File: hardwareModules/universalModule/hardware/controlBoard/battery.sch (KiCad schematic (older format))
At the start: 27 parts

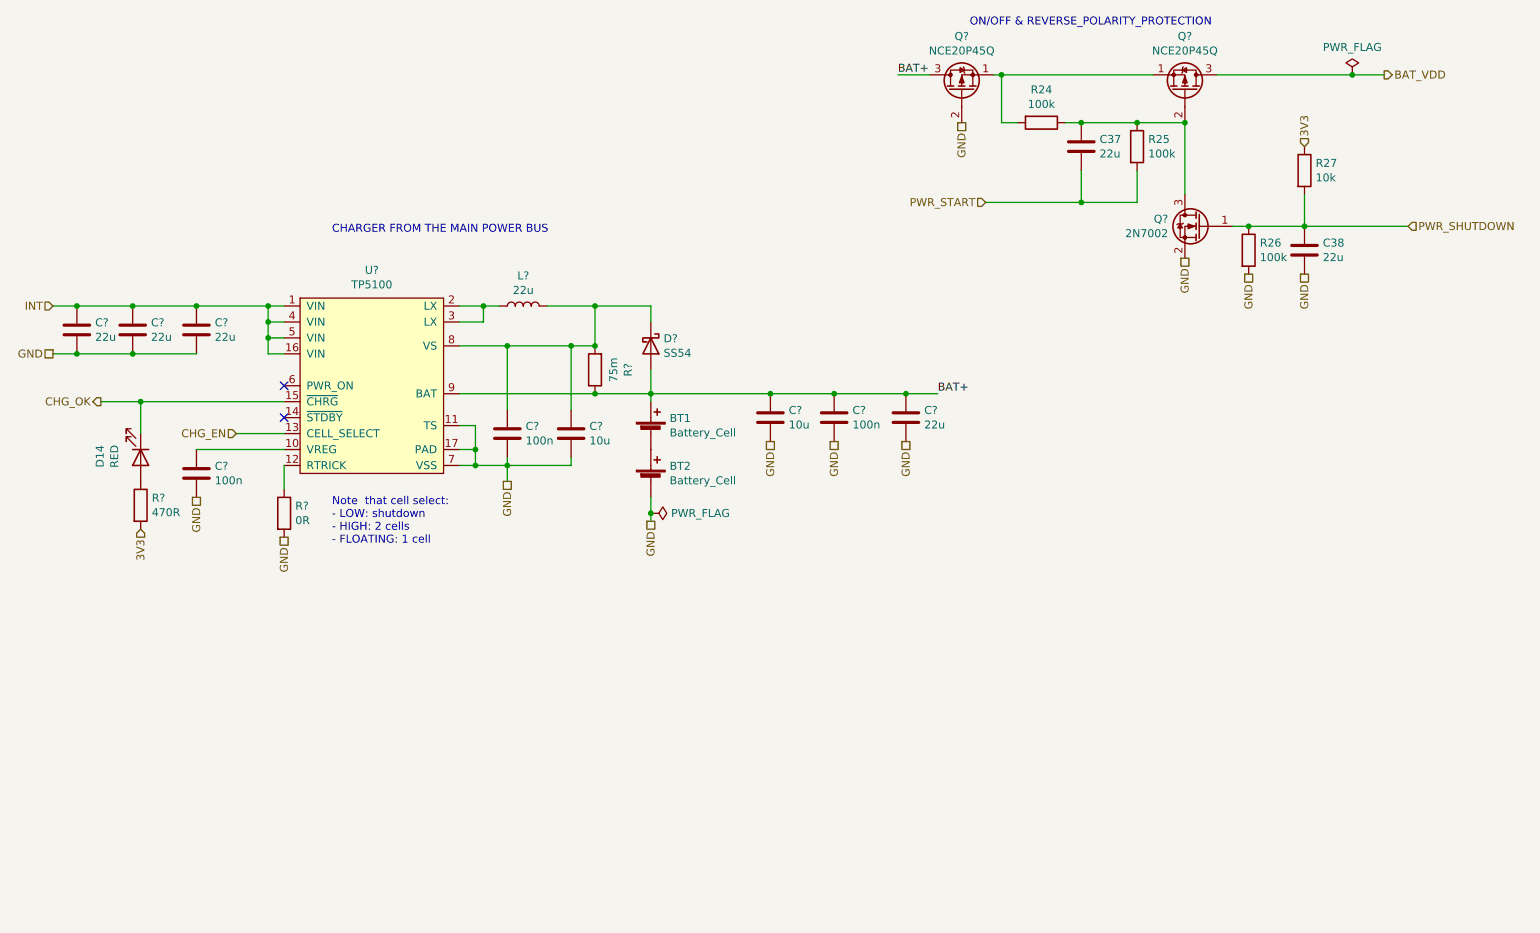
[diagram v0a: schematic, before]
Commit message: universalModule: Draft schematics of the new version of the control board
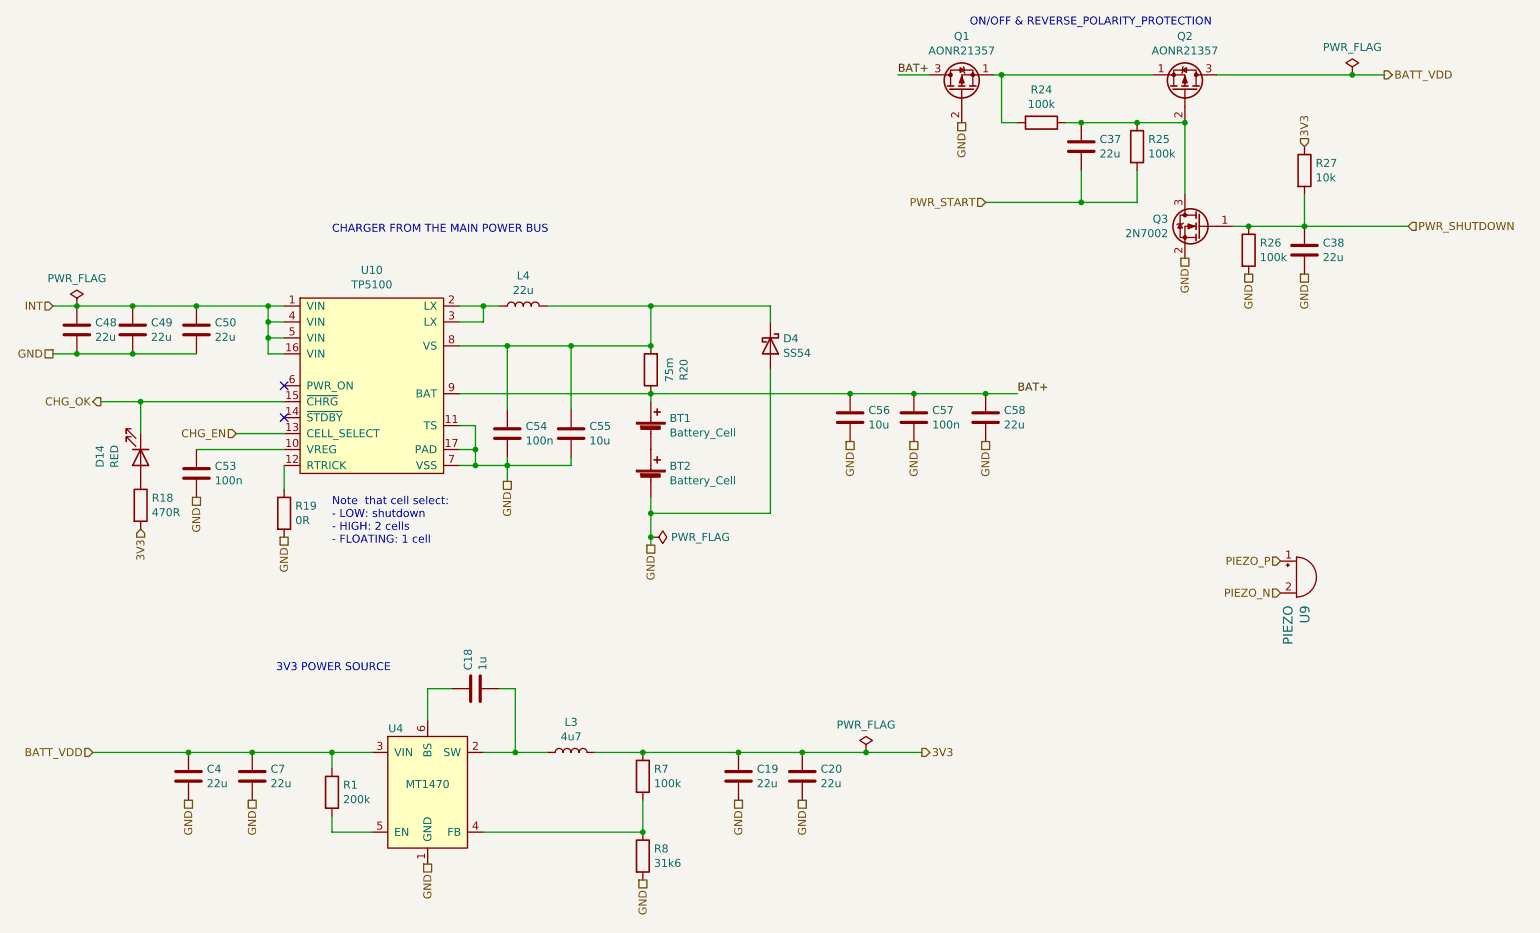
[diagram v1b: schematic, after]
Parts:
- added C18: 1u, Capacitor_SMD:C_0603_1608Metric, symbol Device:C
- added C19, C20, C4, C7: 22u, Capacitor_SMD:C_0805_2012Metric, symbol Device:C
- added L3: 4u7, rofi:SMNR5020, symbol Device:L
- added R1: 200k, Resistor_SMD:R_0402_1005Metric, symbol Device:R
- added R7: 100k, Resistor_SMD:R_0402_1005Metric, symbol Device:R
- added R8: 31k6, Resistor_SMD:R_0402_1005Metric, symbol Device:R
- added U4: MT1470, Package_TO_SOT_SMD:SOT-23-6, symbol rofi:MT1470
- added U9: PIEZO, rofi:CST-931AP, symbol Device:Buzzer
- Q1, Q2: renamed from Q?; value NCE20P45Q -> AONR21357; LCSC C193354 -> C431196
- R18: renamed from R?; footprint (none) -> Resistor_SMD:R_0402_1005Metric
- gave numbers to parts that had none: 15
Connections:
- net 3V3: now also C19.1, C20.1, L3.2, R7.1
- net BAT+: no longer D4.2 (A)
- net GND: now also D4.2 (A), C19.2, C20.2, C4.2, C7.2, R8.2, U4.1 (GND)
- net BAT_VDD renamed BATT_VDD
- net BATT_VDD: now also C4.1, C7.1, R1.1, U4.3 (VIN)
- new net: C18.1, U4.6 (BS)
- new net: C18.2, L3.1, U4.2 (SW)
- new net: R7.2, R8.1, U4.4 (FB)
- new net: R1.2, U4.5 (EN)
- new net PIEZO_N: U9.2 (+)
- new net PIEZO_P: U9.1 (-)
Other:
- note added: "3V3 POWER SOURCE"
- moved on the sheet: C56, C57, C58, D4, R20

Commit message: universalModule: Prepare electronics v0.2
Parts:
- removed C50: 22u, Capacitor_SMD:C_0805_2012Metric, symbol Device:C
- removed C56: 10u, Capacitor_SMD:C_0805_2012Metric, symbol Device:C
- BT1, BT2: #manf (none) -> 2x 1017-1; JLCPCB_IGNORE (none) -> YES
- C18: LCSC C52923 -> C15849
- D14, D4, Q3: JLCPCB_CORRECTION (none) -> 0;0;180
- Q1, Q2: JLCPCB_CORRECTION (none) -> 0;0;-90
- R19: LCSC (none) -> C17168
- R20: LCSC C57963 -> C127704
- R8: value 31k6 -> 22k; LCSC C11463 -> C25768
- U10: JLCPCB_CORRECTION (none) -> 0;0;-90; LCSC (none) -> C379389
- U4: value MT1470 -> SD8942; symbol rofi:MT1470 -> rofi:SD8942; JLCPCB_CORRECTION (none) -> 0;0;180; LCSC (none) -> C250795
- U9: JLCPCB_IGNORE (none) -> YES; MFR_QTY (none) -> 1
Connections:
- net BATT_VDD: now also U4.5 (VIN); no longer U4.3 (VIN)
- net GND: now also U4.2 (GND); no longer U4.1 (GND)
- net BATT_MID: now reaches BT1.2 (-), BT2.1 (+)
- net at C18.1: now also U4.1 (BS); no longer U4.6 (BS)
- net at C18.2, L3.1: now also U4.6 (SW); no longer U4.2 (SW)
- net at R7.2, R8.1: now also U4.3 (FB); no longer U4.4 (FB)
- net at R1.2: now also U4.4 (EN); no longer U4.5 (EN)
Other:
- moved on the sheet: BT2
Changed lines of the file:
@@
 $Descr A4 11693 8268
 encoding utf-8
-Sheet 5 5
+Sheet 5 14
 Title ""
 Date ""
@@
 F 3 "~" H 1950 4150 50  0001 C CNN
 F 4 "C2286" H 1950 4150 50  0001 C CNN "LCSC"
+F 5 "0;0;180" H 1950 4150 50  0001 C CNN "JLCPCB_CORRECTION"
 	1    1950 4150
 	0    1    1    0
@@
 Text HLabel 9250 3000 3    50   UnSpc ~ 0
 GND
-$Comp
-L Device:Q_PMOS_SGD Q2
-U 1 1 5FC760BF
-P 8500 1850
-F 0 "Q2" V 8842 1850 50  0000 C CNN
-F 1 "AONR21357" V 8751 1850 50  0000 C CNN
-F 2 "rofi:DFN3.3X3.3-EP" H 8700 1950 50  0001 C CNN
-F 3 "~" H 8500 1850 50  0001 C CNN
-F 4 "C431196" H 8500 1850 50  0001 C CNN "LCSC"
-	1    8500 1850
-	0    1    -1   0
-$EndComp
 Connection ~ 8500 2050
 $Comp
@@
 F 3 "~" H 7100 1850 50  0001 C CNN
 F 4 "C431196" H 7100 1850 50  0001 C CNN "LCSC"
+F 5 "0;0;-90" V 7100 1850 50  0001 C CNN "JLCPCB_CORRECTION"
 	1    7100 1850
 	0    -1   -1   0
@@
 F 3 "https://www.fairchildsemi.com/datasheets/2N/2N7002.pdf" H 8600 2700 50  0001 L CNN
 F 4 "C8545" H 8600 2700 50  0001 C CNN "LCSC"
+F 5 "0;0;180" H 8600 2700 50  0001 C CNN "JLCPCB_CORRECTION"
 	1    8600 2700
 	-1   0    0    -1
-$EndComp
-$Comp
-L Device:Battery_Cell BT2
-U 1 1 5DFAE964
-P 5150 4300
-F 0 "BT2" H 5268 4396 50  0000 L CNN
-F 1 "Battery_Cell" H 5268 4305 50  0000 L CNN
-F 2 "rofi:BATTERY_18350" V 5150 4360 50  0001 C CNN
-F 3 "~" V 5150 4360 50  0001 C CNN
-F 4 "" H 5150 4300 50  0001 C CNN "#manf"
-	1    5150 4300
-	1    0    0    -1
 $EndComp
 $Comp
@@
 F 2 "rofi:BATTERY_18350" V 5150 4060 50  0001 C CNN
 F 3 "~" V 5150 4060 50  0001 C CNN
-F 4 "" H 5150 4000 50  0001 C CNN "#manf"
+F 4 "2x 1017-1" H 5150 4000 50  0001 C CNN "#manf"
+F 5 "YES" H 5150 4000 50  0001 C CNN "JLCPCB_IGNORE"
 	1    5150 4000
 	1    0    0    -1
@@
 F 2 "Package_DFN_QFN:QFN-16-1EP_4x4mm_P0.65mm_EP2.1x2.1mm" H 3650 3100 50  0001 C CNN
 F 3 "" H 3650 3100 50  0001 C CNN
+F 4 "C379389" H 3400 3700 50  0001 C CNN "LCSC"
+F 5 "0;0;-90" H 3400 3700 50  0001 C CNN "JLCPCB_CORRECTION"
 	1    3400 3700
 	1    0    0    -1
@@
 F 2 "Resistor_SMD:R_1206_3216Metric" V 5080 3600 50  0001 C CNN
 F 3 "~" H 5150 3600 50  0001 C CNN
-F 4 "C57963" V 5150 3600 50  0001 C CNN "LCSC"
+F 4 "C127704" V 5150 3600 50  0001 C CNN "LCSC"
 	1    5150 3600
 	-1   0    0    1
@@
 Text HLabel 5150 4700 3    50   UnSpc ~ 0
 GND
-Wire Wire Line
-	5150 4400 5150 4500
 $Comp
 L power:PWR_FLAG #FLG0103
@@
 Wire Wire Line
 	5150 4650 5150 4700
-Wire Wire Line
-	5150 3800 5150 3750
 Connection ~ 5150 3750
 Text Label 7450 3750 0    50   ~ 0
@@
 F 3 "~" H 5900 3450 50  0001 C CNN
 F 4 "C22452" V 5900 3450 50  0001 C CNN "LCSC"
+F 5 "0;0;180" V 5900 3450 50  0001 C CNN "JLCPCB_CORRECTION"
 	1    5900 3450
 	0    1    1    0
@@
 $EndComp
 $Comp
-L Device:C C56
-U 1 1 5FD18536
-P 6400 3900
-F 0 "C56" H 6515 3946 50  0000 L CNN
-F 1 "10u" H 6515 3855 50  0000 L CNN
-F 2 "Capacitor_SMD:C_0805_2012Metric" H 6438 3750 50  0001 C CNN
-F 3 "~" H 6400 3900 50  0001 C CNN
-F 4 "C15850" H 6400 3900 50  0001 C CNN "LCSC"
-	1    6400 3900
-	1    0    0    -1
-$EndComp
-Connection ~ 6400 3750
-Wire Wire Line
-	6400 3750 6800 3750
-$Comp
 L Device:C C57
 U 1 1 5FD18C0D
@@
 Wire Wire Line
 	6800 3750 7250 3750
-Text HLabel 6400 4050 3    50   UnSpc ~ 0
-GND
 Text HLabel 6800 4050 3    50   UnSpc ~ 0
 GND
@@
 Text HLabel 2300 4400 3    50   UnSpc ~ 0
 GND
-$Comp
-L Device:C C50
-U 1 1 5FD4F2CC
-P 2300 3350
-F 0 "C50" H 2415 3396 50  0000 L CNN
-F 1 "22u" H 2415 3305 50  0000 L CNN
-F 2 "Capacitor_SMD:C_0805_2012Metric" H 2338 3200 50  0001 C CNN
-F 3 "~" H 2300 3350 50  0001 C CNN
-F 4 "GRM21BR61C226ME44L" H 2300 3350 50  0001 C CNN "#manf"
-F 5 "C45783" H 2300 3350 50  0001 C CNN "LCSC"
-	1    2300 3350
-	1    0    0    -1
-$EndComp
-$Comp
-L Device:C C49
-U 1 1 5FD4F8F1
-P 1900 3350
-F 0 "C49" H 2015 3396 50  0000 L CNN
-F 1 "22u" H 2015 3305 50  0000 L CNN
-F 2 "Capacitor_SMD:C_0805_2012Metric" H 1938 3200 50  0001 C CNN
-F 3 "~" H 1900 3350 50  0001 C CNN
-F 4 "GRM21BR61C226ME44L" H 1900 3350 50  0001 C CNN "#manf"
-F 5 "C45783" H 1900 3350 50  0001 C CNN "LCSC"
-	1    1900 3350
-	1    0    0    -1
-$EndComp
 $Comp
 L Device:C C48
@@
 Wire Wire Line
 	2850 3200 2750 3200
-Wire Wire Line
-	2300 3200 1900 3200
-Connection ~ 2300 3200
-Wire Wire Line
-	1900 3200 1550 3200
-Connection ~ 1900 3200
 Text HLabel 1400 3200 0    50   Input ~ 0
 INT
@@
 Connection ~ 1550 3200
 Wire Wire Line
-	2300 3500 1900 3500
-Wire Wire Line
-	1900 3500 1550 3500
-Connection ~ 1900 3500
-Wire Wire Line
 	1550 3500 1400 3500
-Connection ~ 1550 3500
 Text HLabel 1400 3500 0    50   UnSpc ~ 0
 GND
@@
 	2750 3300 2750 3200
 Connection ~ 2750 3200
-Wire Wire Line
-	2750 3200 2300 3200
 Wire Wire Line
 	2750 3300 2850 3300
@@
 F 2 "Resistor_SMD:R_0402_1005Metric" V 2780 4500 50  0001 C CNN
 F 3 "~" H 2850 4500 50  0001 C CNN
+F 4 "C17168" H 2850 4500 50  0001 C CNN "LCSC"
 	1    2850 4500
 	1    0    0    -1
@@
 PIEZO_N
 Wire Wire Line
-	5150 3750 6400 3750
-Wire Wire Line
 	5150 3200 5900 3200
 Wire Wire Line
@@
 F 2 "Capacitor_SMD:C_0603_1608Metric" H 4088 5450 50  0001 C CNN
 F 3 "~" H 4050 5600 50  0001 C CNN
-F 4 "C52923" H 4050 5600 50  0001 C CNN "LCSC"
+F 4 "C15849" H 4050 5600 50  0001 C CNN "LCSC"
 	1    4050 5600
 	0    -1   -1   0
@@
 AR Path="/5DFADF1E/6110B98B" Ref="R8"  Part="1"
 F 0 "R8" H 5170 6696 50  0000 L CNN
-F 1 "31k6" H 5170 6605 50  0000 L CNN
+F 1 "22k" H 5170 6605 50  0000 L CNN
 F 2 "Resistor_SMD:R_0402_1005Metric" V 5030 6650 50  0001 C CNN
 F 3 "~" H 5100 6650 50  0001 C CNN
-F 4 "C11463" H 5100 6650 50  0001 C CNN "LCSC"
+F 4 "C25768" H 5100 6650 50  0001 C CNN "LCSC"
 	1    5100 6650
 	1    0    0    -1
 $EndComp
 Wire Wire Line
-	4100 6500 5100 6500
-Wire Wire Line
 	5100 6500 5100 6300
-Connection ~ 5100 6500
 $Comp
 L Device:R R?
@@
 	3150 6100 3150 6000
 Wire Wire Line
-	3150 6000 3400 6000
-Wire Wire Line
 	3150 6400 3150 6500
 Wire Wire Line
@@
 Wire Wire Line
 	2650 6000 3150 6000
-Connection ~ 3150 6000
 Wire Wire Line
 	2650 6000 2250 6000
 Connection ~ 2650 6000
 Connection ~ 2250 6000
-Text HLabel 1650 6000 0    50   Input ~ 0
-BATT_VDD
-$Comp
-L rofi:MT1470 U?
+$Comp
+L rofi:SD8942 U?
 U 1 1 6110B9D4
 P 3750 6100
@@
 AR Path="/5DFADF1E/6110B9D4" Ref="U4"  Part="1"
 F 0 "U4" H 3550 6350 50  0000 C CNN
-F 1 "MT1470" H 3750 6000 50  0000 C CNN
+F 1 "SD8942" H 3750 6000 50  0000 C CNN
 F 2 "Package_TO_SOT_SMD:SOT-23-6" H 3750 5750 50  0001 C CNN
 F 3 "" H 3750 6100 50  0001 C CNN
+F 4 "C250795" H 3750 6100 50  0001 C CNN "LCSC"
+F 5 "0;0;180" H 3750 6100 50  0001 C CNN "JLCPCB_CORRECTION"
 	1    3750 6100
 	1    0    0    -1
@@
 F 3 "" H 9200 4900 60  0000 C CNN
 F 4 "CST-931AP" V 9200 4900 50  0001 C CNN "MFR"
+F 5 "1" H 9200 4900 50  0001 C CNN "MFR_QTY"
+F 6 "YES" H 9200 4900 50  0001 C CNN "JLCPCB_IGNORE"
 	1    9200 4900
 	1    0    0    -1
@@
 	1    0    0    -1
 $EndComp
+Connection ~ 1550 3500
+Wire Wire Line
+	1900 3500 1550 3500
+Wire Wire Line
+	1900 3200 2750 3200
+Wire Wire Line
+	1900 3200 1550 3200
+Connection ~ 1900 3200
+$Comp
+L Device:C C49
+U 1 1 5FD4F8F1
+P 1900 3350
+F 0 "C49" H 2015 3396 50  0000 L CNN
+F 1 "22u" H 2015 3305 50  0000 L CNN
+F 2 "Capacitor_SMD:C_0805_2012Metric" H 1938 3200 50  0001 C CNN
+F 3 "~" H 1900 3350 50  0001 C CNN
+F 4 "GRM21BR61C226ME44L" H 1900 3350 50  0001 C CNN "#manf"
+F 5 "C45783" H 1900 3350 50  0001 C CNN "LCSC"
+	1    1900 3350
+	1    0    0    -1
+$EndComp
+Wire Wire Line
+	5150 3750 6800 3750
+Wire Wire Line
+	5150 4450 5150 4500
+$Comp
+L Device:Battery_Cell BT2
+U 1 1 5DFAE964
+P 5150 4350
+F 0 "BT2" H 5268 4446 50  0000 L CNN
+F 1 "Battery_Cell" H 5268 4355 50  0000 L CNN
+F 2 "rofi:BATTERY_18350" V 5150 4410 50  0001 C CNN
+F 3 "~" V 5150 4410 50  0001 C CNN
+F 4 "2x 1017-1" H 5150 4350 50  0001 C CNN "#manf"
+F 5 "YES" H 5150 4350 50  0001 C CNN "JLCPCB_IGNORE"
+	1    5150 4350
+	1    0    0    -1
+$EndComp
+Wire Wire Line
+	5150 3800 5150 3750
+Wire Wire Line
+	5150 4100 5150 4150
+Wire Wire Line
+	5150 4150 5350 4150
+Connection ~ 5150 4150
+Text Label 5350 4150 0    50   ~ 0
+BATT_MID
+$Comp
+L Device:Q_PMOS_SGD Q2
+U 1 1 5FC760BF
+P 8500 1850
+F 0 "Q2" V 8842 1850 50  0000 C CNN
+F 1 "AONR21357" V 8751 1850 50  0000 C CNN
+F 2 "rofi:DFN3.3X3.3-EP" H 8700 1950 50  0001 C CNN
+F 3 "~" H 8500 1850 50  0001 C CNN
+F 4 "C431196" H 8500 1850 50  0001 C CNN "LCSC"
+F 5 "0;0;-90" V 8500 1850 50  0001 C CNN "JLCPCB_CORRECTION"
+	1    8500 1850
+	0    1    -1   0
+$EndComp
+Wire Wire Line
+	4100 6500 5100 6500
+Connection ~ 5100 6500
+Wire Wire Line
+	3400 6000 3150 6000
+Connection ~ 3150 6000
+Text HLabel 1650 6000 0    50   Input ~ 0
+BATT_VDD
 $EndSCHEMATC

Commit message: universalModule: Add final pre-production tweaks
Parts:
- D14, D4: JLCPCB_CORRECTION 0;0;180 -> (none)
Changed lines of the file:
@@
 F 3 "~" H 1950 4150 50  0001 C CNN
 F 4 "C2286" H 1950 4150 50  0001 C CNN "LCSC"
-F 5 "0;0;180" H 1950 4150 50  0001 C CNN "JLCPCB_CORRECTION"
 	1    1950 4150
 	0    1    1    0
@@
 F 3 "~" H 5900 3450 50  0001 C CNN
 F 4 "C22452" V 5900 3450 50  0001 C CNN "LCSC"
-F 5 "0;0;180" V 5900 3450 50  0001 C CNN "JLCPCB_CORRECTION"
 	1    5900 3450
 	0    1    1    0
